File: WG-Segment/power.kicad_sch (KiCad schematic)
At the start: 0 parts

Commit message: Design full circuit
Still need to run ERC
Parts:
- added C301: 100n, Capacitor_SMD:C_0402_1005Metric_Pad0.74x0.62mm_HandSolder, symbol Device:C
- added C302: 10u, Capacitor_SMD:C_0805_2012Metric_Pad1.18x1.45mm_HandSolder, symbol Device:C
- added C303, C304: 22u, Capacitor_SMD:C_0805_2012Metric_Pad1.18x1.45mm_HandSolder, symbol Device:C
- added C305, C306: 1u/10V, Capacitor_SMD:C_0402_1005Metric_Pad0.74x0.62mm_HandSolder, symbol Device:C
- added C307, C309: 2.2u, Capacitor_SMD:C_0402_1005Metric_Pad0.74x0.62mm_HandSolder, symbol Device:C
- added C308: 1n, Capacitor_SMD:C_0402_1005Metric_Pad0.74x0.62mm_HandSolder, symbol Device:C
- added L301: 4.7uH, WordGameLib:Murata_1255AY, symbol Device:L
- added R302: 50R, Resistor_SMD:R_0402_1005Metric_Pad0.72x0.64mm_HandSolder, symbol Device:R
- added U301: AP63205WU, Package_TO_SOT_SMD:TSOT-23-6, symbol Regulator_Switching:AP63205WU
- added U302: MIC5504-3.3YM5, Package_TO_SOT_SMD:SOT-23-5_HandSoldering, symbol Regulator_Linear:MIC5504-3.3YM5
- added U303: MCP1501T-33E, Package_TO_SOT_SMD:SOT-23-6, symbol Reference_Voltage:MCP1501-33xCH
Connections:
- new net: C309.1, R302.2
- new net: C301.2, L301.1, U301.5 (SW)
- new net: C301.1, U301.6 (BST)
- new net +12V: C302.1, U301.2 (EN), U301.3 (IN)
- new net +3V3: C306.1, U302.5 (VOUT)
- new net +5V: C303.1, C304.1, C305.1, C307.1, L301.2, U301.1 (FB), U302.1 (VIN), U302.3 (EN), U303.4 (~{SHDN}), U303.6 (VDD)
- new net GND: C302.2, C303.2, C304.2, C305.2, C306.2, C307.2, C308.1, C309.2, U301.4 (GND), U302.2 (GND), U303.2 (GND), U303.3 (GND), U303.5 (GND)
- new net VREF: C308.2, R302.1, U303.1 (OUT)
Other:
- note added: "3.8-32V input. 5V @ 2A output"
- note added: "5V input. 3V3 0.1% @ 20mA output"
- note added: "5V input. 3V3 @ 300mA output"

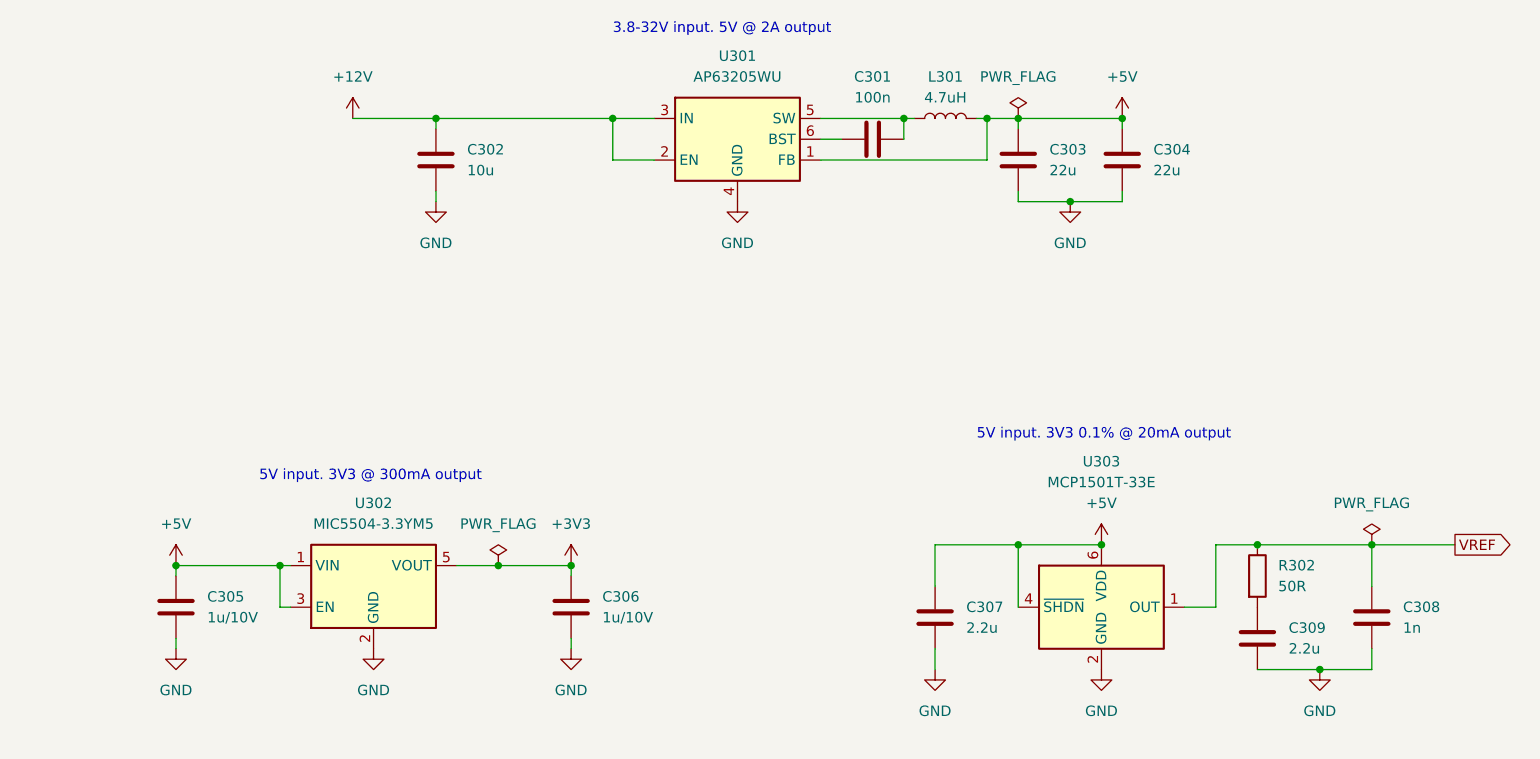
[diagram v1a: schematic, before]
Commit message: Add level shifter to LED data input
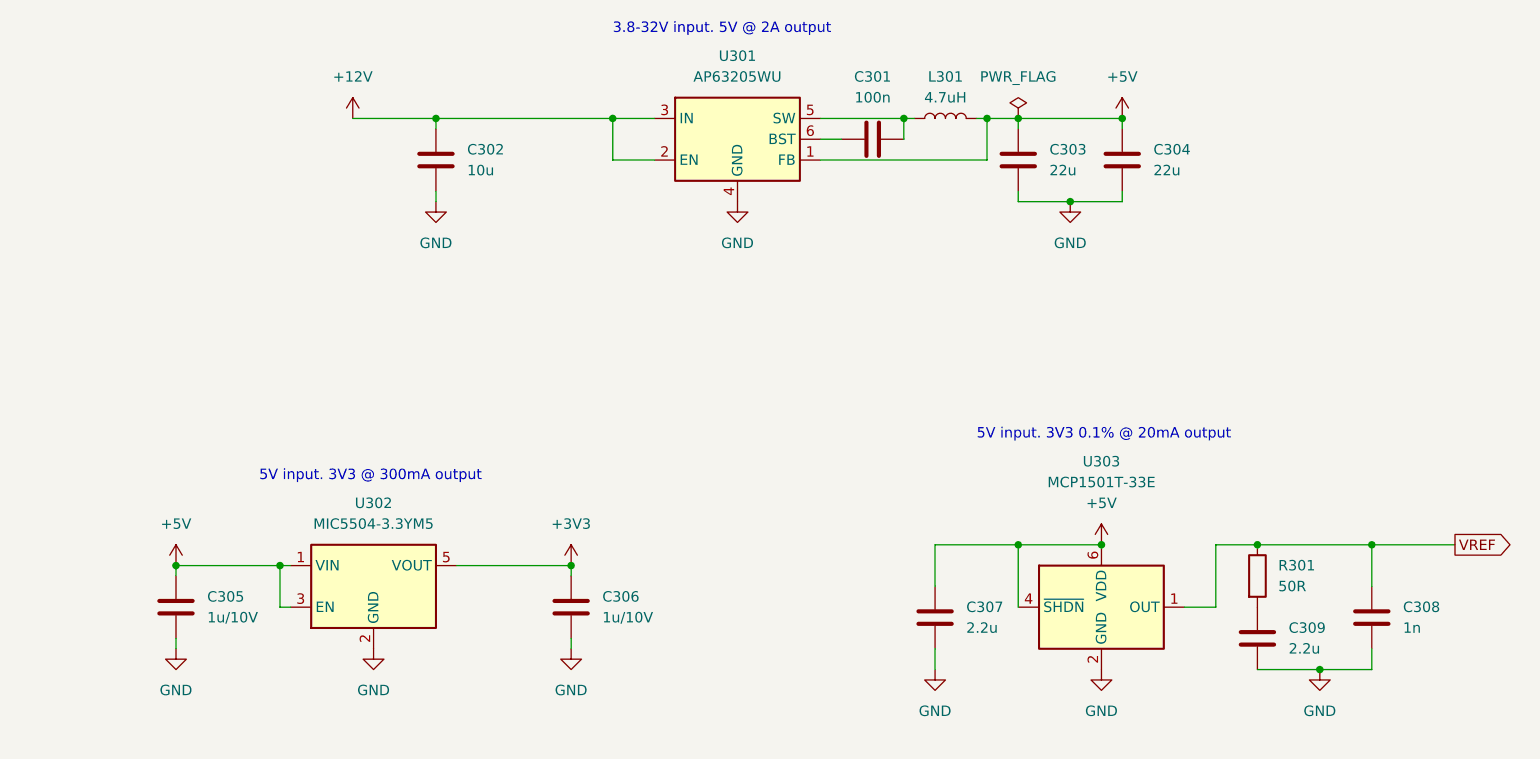
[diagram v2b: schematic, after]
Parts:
- renumbered R302 to R301
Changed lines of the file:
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@@
   (junction (at 161.29 69.85) (diameter 0) (color 0 0 0 0)
   )
-  (junction (at 111.76 124.46) (diameter 0) (color 0 0 0 0)
-  )
   (junction (at 85.09 124.46) (diameter 0) (color 0 0 0 0)
   )
@@
     (stroke (width 0) (type default))
   )
-  (wire (pts (xy 111.76 124.46) (xy 120.65 124.46))
-    (stroke (width 0) (type default))
-  )
   (wire (pts (xy 151.13 69.85) (xy 161.29 69.85))
     (stroke (width 0) (type default))
@@
     (stroke (width 0) (type default))
   )
-  (wire (pts (xy 106.68 124.46) (xy 111.76 124.46))
+  (wire (pts (xy 106.68 124.46) (xy 120.65 124.46))
     (stroke (width 0) (type default))
   )
@@
   (symbol (lib_id "Device:R") (at 204.47 125.73 0) (unit 1)
     (in_bom yes) (on_board yes) (dnp no) (fields_autoplaced)
-    (property "Reference" "R302" (at 207.01 124.46 0)
+    (property "Reference" "R301" (at 207.01 124.46 0)
       (effects (font (size 1.27 1.27)) (justify left))
     )
@@
       (project "WG-Segment"
         (path "/9a5339e6-f970-4986-a2cb-f70ab323b7e1/59659887-599e-4b15-819a-7d99a27b9ab4"
-          (reference "R302") (unit 1)
+          (reference "R301") (unit 1)
         )
       )
@@
     )
   )
-  (symbol (lib_id "power:PWR_FLAG") (at 218.44 121.92 0) (unit 1)
-    (in_bom yes) (on_board yes) (dnp no) (fields_autoplaced)
-    (property "Reference" "#FLG0302" (at 218.44 120.015 0)
-      (effects (font (size 1.27 1.27)) hide)
-    )
-    (property "Value" "PWR_FLAG" (at 218.44 116.84 0)
-      (effects (font (size 1.27 1.27)))
-    )
-    (property "Footprint" "" (at 218.44 121.92 0)
-      (effects (font (size 1.27 1.27)) hide)
-    )
-    (property "Datasheet" "~" (at 218.44 121.92 0)
-      (effects (font (size 1.27 1.27)) hide)
-    )
-    (pin "1")
-    (instances
-      (project "WG-Segment"
-        (path "/9a5339e6-f970-4986-a2cb-f70ab323b7e1/59659887-599e-4b15-819a-7d99a27b9ab4"
-          (reference "#FLG0302") (unit 1)
-        )
-      )
-    )
-  )
   (symbol (lib_id "power:+5V") (at 187.96 69.85 0) (unit 1)
     (in_bom yes) (on_board yes) (dnp no) (fields_autoplaced)
@@
         )
       )
-    )
-  )
-  (symbol (lib_id "power:PWR_FLAG") (at 111.76 124.46 0) (unit 1)
-    (in_bom yes) (on_board yes) (dnp no) (fields_autoplaced)
-    (property "Reference" "#FLG0303" (at 111.76 122.555 0)
-      (effects (font (size 1.27 1.27)) hide)
-    )
-    (property "Value" "PWR_FLAG" (at 111.76 119.38 0)
-      (effects (font (size 1.27 1.27)))
-    )
-    (property "Footprint" "" (at 111.76 124.46 0)
-      (effects (font (size 1.27 1.27)) hide)
-    )
-    (property "Datasheet" "~" (at 111.76 124.46 0)
-      (effects (font (size 1.27 1.27)) hide)
-    )
-    (pin "1")
-    (instances
-      (project "WG-Segment"
-        (path "/9a5339e6-f970-4986-a2cb-f70ab323b7e1/59659887-599e-4b15-819a-7d99a27b9ab4"
-          (reference "#FLG0303") (unit 1)
-        )
-      )

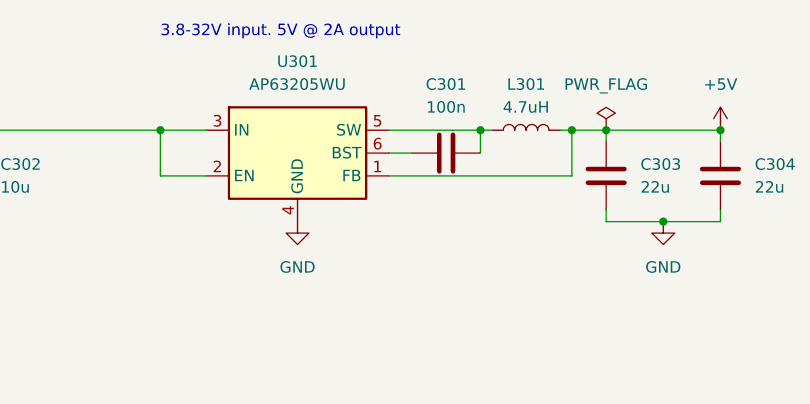
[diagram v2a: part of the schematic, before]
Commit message: Position power circuitry
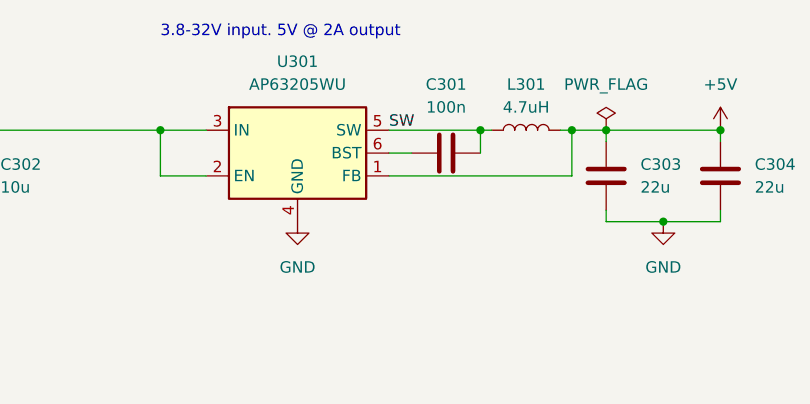
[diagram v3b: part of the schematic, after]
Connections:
- net SW: now reaches C301.2, L301.1, U301.5 (SW)
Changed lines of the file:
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@@
+    (effects (font (size 1.27 1.27)) (justify left bottom))
+  )
+  (label "SW" (at 151.13 69.85 0) (fields_autoplaced)
     (effects (font (size 1.27 1.27)) (justify left bottom))
   )

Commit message: Fix build issues
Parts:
- C301: value 100n -> 0.1u; Desc (none) -> CAP CER 0.1uF 10V 0402
- C302: Desc (none) -> CAP CER 10uF 25V 0805 low-ESR
- C303, C304: Desc (none) -> CAP CER 22u 10V 0805 low-ESR
- C305, C306: value 1u/10V -> 1u,10V; Desc (none) -> CAP CER 1uF 10V 0402
- C307, C309: Desc (none) -> CAP CER 2.2uF 10V 0402
- C308: Desc (none) -> CAP CER 1nF 10V 0402
- L301: Desc (none) -> IND 4.7uH <100mOhm >2.5A
- R301: Desc (none) -> RES 50R 1/10W 1% 0402
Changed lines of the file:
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@@
       (effects (font (size 1.27 1.27)) (justify left))
     )
-    (property "Value" "1u/10V" (at 76.2 130.81 0)
+    (property "Value" "1u,10V" (at 76.2 130.81 0)
       (effects (font (size 1.27 1.27)) (justify left))
     )
@@
       (effects (font (size 1.27 1.27)) hide)
     )
-    (property "Description" "CAP CER 1uF 10V 0402" (at 72.39 129.54 0)
+    (property "Desc" "CAP CER 1uF 10V 0402" (at 72.39 129.54 0)
       (effects (font (size 1.27 1.27)) hide)
     )
@@
     )
     (property "Manufacturer" "Microchip Technology" (at 96.52 127 0)
-      (effects (font (size 1.27 1.27)) hide)
-    )
-    (property "Description" "" (at 96.52 127 0)
       (effects (font (size 1.27 1.27)) hide)
     )
@@
       (effects (font (size 1.27 1.27)) hide)
     )
-    (property "Description" "CAP CER 10uF 25V 0805 low-ESR" (at 104.14 74.93 0)
+    (property "Desc" "CAP CER 10uF 25V 0805 low-ESR" (at 104.14 74.93 0)
       (effects (font (size 1.27 1.27)) hide)
     )
@@
     )
     (property "Manufacturer" "Microchip Technology" (at 185.42 129.54 0)
-      (effects (font (size 1.27 1.27)) hide)
-    )
-    (property "Description" "" (at 185.42 129.54 0)
       (effects (font (size 1.27 1.27)) hide)
     )
@@
       (effects (font (size 1.27 1.27)) (justify left))
     )
-    (property "Value" "1u/10V" (at 124.46 130.81 0)
+    (property "Value" "1u,10V" (at 124.46 130.81 0)
       (effects (font (size 1.27 1.27)) (justify left))
     )
@@
       (effects (font (size 1.27 1.27)) hide)
     )
-    (property "Description" "CAP CER 1uF 10V 0402" (at 120.65 129.54 0)
+    (property "Desc" "CAP CER 1uF 10V 0402" (at 120.65 129.54 0)
       (effects (font (size 1.27 1.27)) hide)
     )
@@
       (effects (font (size 1.27 1.27)) hide)
     )
-    (property "Description" "CAP CER 2.2uF 10V 0402" (at 204.47 133.35 0)
+    (property "Desc" "CAP CER 2.2uF 10V 0402" (at 204.47 133.35 0)
       (effects (font (size 1.27 1.27)) hide)
     )
@@
       (effects (font (size 1.27 1.27)) hide)
     )
-    (property "Description" "CAP CER 1nF 10V 0402" (at 218.44 130.81 0)
+    (property "Desc" "CAP CER 1nF 10V 0402" (at 218.44 130.81 0)
       (effects (font (size 1.27 1.27)) hide)
     )
@@
       (effects (font (size 1.27 1.27)) hide)
     )
-    (property "Description" "CAP CER 2.2uF 10V 0402" (at 165.1 130.81 0)
+    (property "Desc" "CAP CER 2.2uF 10V 0402" (at 165.1 130.81 0)
       (effects (font (size 1.27 1.27)) hide)
     )
@@
       (effects (font (size 1.27 1.27)) hide)
     )
-    (property "Description" "CAP CER 22u 10V 0805 low-ESR" (at 187.96 74.93 0)
+    (property "Desc" "CAP CER 22u 10V 0805 low-ESR" (at 187.96 74.93 0)
       (effects (font (size 1.27 1.27)) hide)
     )
@@
       (effects (font (size 1.27 1.27)) hide)
     )
-    (property "Description" "RES 50R 1/10W 1% 0402" (at 204.47 125.73 0)
+    (property "Desc" "RES 50R 1/10W 1% 0402" (at 204.47 125.73 0)
       (effects (font (size 1.27 1.27)) hide)
     )
@@
       (effects (font (size 1.27 1.27)) hide)
     )
-    (property "Description" "CAP CER 22u 10V 0805 low-ESR" (at 175.26 74.93 0)
+    (property "Desc" "CAP CER 22u 10V 0805 low-ESR" (at 175.26 74.93 0)
       (effects (font (size 1.27 1.27)) hide)
     )
@@
       (effects (font (size 1.27 1.27)))
     )
-    (property "Value" "100n" (at 157.48 67.31 90)
+    (property "Value" "0.1u" (at 157.48 67.31 90)
       (effects (font (size 1.27 1.27)))
     )
@@
       (effects (font (size 1.27 1.27)) hide)
     )
-    (property "Description" "CAP CER 100nF 10V 0402" (at 157.48 72.39 0)
+    (property "Desc" "CAP CER 0.1uF 10V 0402" (at 157.48 72.39 0)
       (effects (font (size 1.27 1.27)) hide)
     )
@@
       (effects (font (size 1.27 1.27)) hide)
     )
-    (property "Description" "IND 4.7uH <100mOhm >2.5A" (at 166.37 69.85 0)
-      (effects (font (size 1.27 1.27)) hide)
-    )
+    (property "Desc" "IND 4.7uH <100mOhm >2.5A" (at 166.37 69.85 0)
+      (effects (font (size 1.27 1.27)) hide)
+    )

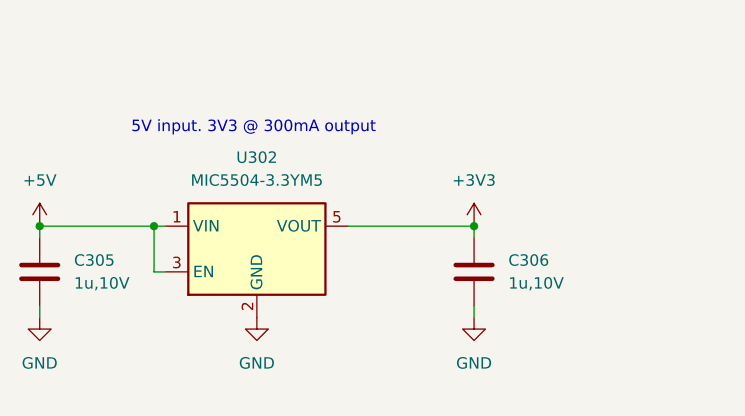
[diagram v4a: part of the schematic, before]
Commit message: Change component value
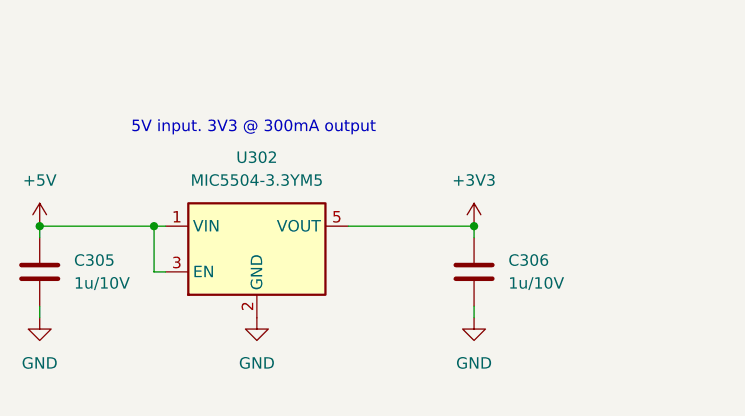
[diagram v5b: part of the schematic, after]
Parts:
- C305, C306: value 1u,10V -> 1u/10V
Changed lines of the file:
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@@
       (effects (font (size 1.27 1.27)) (justify left))
     )
-    (property "Value" "1u,10V" (at 76.2 130.81 0)
+    (property "Value" "1u/10V" (at 76.2 130.81 0)
       (effects (font (size 1.27 1.27)) (justify left))
     )
@@
       (effects (font (size 1.27 1.27)) (justify left))
     )
-    (property "Value" "1u,10V" (at 124.46 130.81 0)
-      (effects (font (size 1.27 1.27)) (justify left))
-    )
+    (property "Value" "1u/10V" (at 124.46 130.81 0)
+      (effects (font (size 1.27 1.27)) (justify left))
+    )

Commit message: Update parts to ones in JLCPCB library
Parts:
- removed C308: 1n, Capacitor_SMD:C_0402_1005Metric_Pad0.74x0.62mm_HandSolder, symbol Device:C
- removed C309: 2.2u, Capacitor_SMD:C_0402_1005Metric_Pad0.74x0.62mm_HandSolder, symbol Device:C
- removed R301: 50R, Resistor_SMD:R_0402_1005Metric_Pad0.72x0.64mm_HandSolder, symbol Device:R
- removed U303: MCP1501T-33E, Package_TO_SOT_SMD:SOT-23-6, symbol Reference_Voltage:MCP1501-33xCH
- added D301: SS34, Diode_SMD:D_SMA, symbol Diode:SS34
- added U303: REF3033, Package_TO_SOT_SMD:SOT-23, symbol Reference_Voltage:REF3033
- C307: value 2.2u -> 470n
- U301: now not fitted
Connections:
- net +12V: now also D301.2 (A); no longer C302.1, U301.2 (EN), U301.3 (IN)
- net +5V: now also U303.1 (IN)
- net GND: now also U303.3 (GND)
- net VREF: now also U303.2 (OUT)
- new net: C302.1, D301.1 (K), U301.2 (EN), U301.3 (IN)
